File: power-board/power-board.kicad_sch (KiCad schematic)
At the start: 0 parts

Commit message: esp8266 module
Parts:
- added BT1: Battery_Cell, symbol Device:Battery_Cell
- added P1: USB_C_Plug_USB2.0, symbol Connector:USB_C_Plug_USB2.0
- added U1: AP9101CK6, Package_TO_SOT_SMD:SOT-23-6, symbol Battery_Management:AP9101CK6
- added U2: AP130-33Y, Package_TO_SOT_SMD:SOT-89-3, symbol Regulator_Linear:AP130-33Y
- added U3: MCP73831-3-OT, Package_TO_SOT_SMD:SOT-23-5, symbol Battery_Management:MCP73831-3-OT
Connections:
- new net: P1.A1 (GND), P1.A12 (GND), P1.B1 (GND), P1.B12 (GND)
- new net: P1.A4 (VBUS), P1.A9 (VBUS), P1.B4 (VBUS), P1.B9 (VBUS)

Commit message: initial diagram
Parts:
- added C1: 100n, symbol Device:C
- added C2: 1n, symbol Device:C
- added C3, C4: 4u7, symbol Device:C
- added C5: 1u, symbol Device:C
- added C6: 10u, symbol Device:C
- added C7, C8: 1000u, symbol Device:C_Polarized
- added F1: 2A slow, symbol Device:Fuse
- added J1: RGB matrix, symbol Connector_Generic:Conn_01x03
- added Q1, Q2: AOB2146L, Package_TO_SOT_SMD:TO-263-2, symbol Transistor_FET:IRFS4115
- added R1: 330, symbol Device:R
- added R10, R9: 5k1, symbol Device:R
- added R2: 2k7, symbol Device:R
- added R3: 1k, symbol Device:R
- added R4: 3k3, symbol Device:R
- added R5: 10k, symbol Device:R
- added R6: 100k, symbol Device:R
- added R7: LDR03, OptoDevice:R_LDR_10x8.5mm_P7.6mm_Vertical, symbol Sensor_Optical:LDR03
- added R8: 470, symbol Device:R
- added SW1: On, symbol Switch:SW_SPST
- added SW2: Mode, symbol Switch:SW_SPST
- added U4: ESP8266-NodeM, symbol rgb_matrix:ESP8266-NodeM
- BT1: value Battery_Cell -> 18650
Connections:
- net +3V3: now reaches U2.1 (VO)
- net +3V3: now also C6.1, C7.1, R5.1, R7.1, U4. (A0)
- net GND: now reaches U2.2 (GND)
- net GND: now also P1.A1 (GND), P1.A12 (GND), P1.B1 (GND), P1.B12 (GND), U3.2 (V_{SS}), C2.2, C3.2, C4.2, C5.2, C6.2, C7.2, C8.2, J1.1 (Pin_1), Q1.3 (S), R10.2, R2.2, R3.1, R4.2, R6.2, R9.2, SW2.1 (A), U4. (A0)
- net +VSW: now reaches U2.3 (VI)
- net +VSW: now also C5.1, C8.1, J1.3 (Pin_3), SW1.2 (B)
- net at BT1.1 (+): now also F1.2
- net BAT-: now reaches BT1.2 (-)
- net BAT-: now also U1.6 (VSS), C1.2, Q2.3 (S)
- net at P1.A4 (VBUS), P1.A9 (VBUS), P1.B4 (VBUS)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: now also U3.4 (V_{DD}), C3.1
- net at P1.A5 (CC): now also R10.1
- net at P1.B5 (VCONN): now also R9.1
- net at P1.SH (SHIELD): now also C2.1, R3.2
- net at U3.3 (V_{BAT}): now also C4.1, F1.1, R1.1, SW1.1 (A)
- net at U3.5 (PROG): now also R4.1
- net at U1.1 (DO): now also Q1.1 (G)
- net at U1.2 (VM): now also R2.1
- net at U1.3 (CO): now also Q2.1 (G)
- net at U1.5 (VDD): now also C1.1, R1.2
- new net: R6.1, R7.2, U4. (A0)
- new net: R5.2, SW2.2 (B), U4. (A0)
- new net: R8.2, U4. (A0)
- new net: Q1.2 (D), Q2.2 (D)
- new net: J1.2 (Pin_2), R8.1
- no-connect marks 0 -> 6
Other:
- note added: "Power must be directly connected to all four panels"
- note added: "Should mechanically block USB input when On"
- note added: "star ground"
- moved on the sheet: BT1, P1, U1, U2, U3

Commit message: esp legs
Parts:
- removed J1: RGB matrix, symbol Connector_Generic:Conn_01x03
- added J1: Conn_01x01, symbol Connector_Generic:Conn_01x01
- added J2, J3, J4, J5: Conn_01x02, symbol Connector_Generic:Conn_01x02
- C2: value 1n -> 1n/50V
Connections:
- net +3V3: now also U4.1 (3V3), U4.10 (3V3), U4.26 (3V3); no longer U4. (A0)
- net +VSW: now also J2.1 (Pin_1), J3.1 (Pin_1), J4.1 (Pin_1), J5.1 (Pin_1)
- net GND: now also U4.2 (GND), U4.25 (GND), U4.29 (GND), U4.9 (GND), J2.2 (Pin_2), J3.2 (Pin_2), J4.2 (Pin_2), J5.2 (Pin_2); no longer U4. (A0)
- net at R6.1, R7.2: now also U4.16 (A0); no longer U4. (A0)
- net at R5.2, SW2.2 (B): now also U4.14 (D1); no longer U4. (A0)
- net at R8.2: now also U4.13 (D2); no longer U4. (A0)
- net at R8.1: now also J1.1 (Pin_1)
- no-connect marks 6 -> 4
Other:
- moved on the sheet: C8

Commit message: usb
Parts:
- removed J1: Conn_01x01, symbol Connector_Generic:Conn_01x01
- removed J5: Conn_01x02, symbol Connector_Generic:Conn_01x02
- removed P1: USB_C_Plug_USB2.0, symbol Connector:USB_C_Plug_USB2.0
- added J1: USB_C, Connector_USB:USB_C_Receptacle_GCT_USB4125-xx-x-0190_6P_TopMnt_Horizontal, symbol Connector:USB_C_Receptacle_PowerOnly_6P
- added J6: Conn_01x03, TerminalBlock_Phoenix:TerminalBlock_Phoenix_PT-1,5-3-3.5-H_1x03_P3.50mm_Horizontal, symbol Connector_Generic:Conn_01x03
- BT1, J2, J3, J4: footprint (none) -> TerminalBlock_Phoenix:TerminalBlock_Phoenix_PT-1,5-2-5.0-H_1x02_P5.00mm_Horizontal
- C1, C2, C3, C4, C5, C6: footprint (none) -> Capacitor_SMD:C_0805_2012Metric_Pad1.18x1.45mm_HandSolder
- C7, C8: footprint (none) -> Capacitor_THT:CP_Radial_D12.5mm_P5.00mm
- F1: footprint (none) -> Fuse:Fuseholder_Cylinder-5x20mm_Schurter_0031_8201_Horizontal_Open
- R1, R10, R2, R3, R4, R5, R6, R8, R9: footprint (none) -> Resistor_SMD:R_0805_2012Metric_Pad1.20x1.40mm_HandSolder
- U4: footprint (none) -> RF_Module:ESP32-C3-DevKitM-1
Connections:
- net +VSW: now also J6.1 (Pin_1)
- net GND: now also J1.A12 (GND), J1.B12 (GND), J6.3 (Pin_3)
- net at R9.1: now also J1.B5 (CC2)
- net at R8.1: now also J6.2 (Pin_2)
- net at R10.1: now also J1.A5 (CC1)
- net at C2.1, R3.2: now also J1.SH (SHIELD)
- net at C3.1, U3.4 (V_{DD}): now also J1.A9 (VBUS), J1.B9 (VBUS)
- no-connect marks 4 -> 2
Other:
- moved on the sheet: C2, C7, R10, R3, R5, R6, R7, R8, R9, SW2, U4

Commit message: rough pcb layout
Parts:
- removed BT1: 18650, TerminalBlock_Phoenix:TerminalBlock_Phoenix_PT-1,5-2-5.0-H_1x02_P5.00mm_Horizontal, symbol Device:Battery_Cell
- removed SW2: Mode, symbol Switch:SW_SPST
- added C9: 100n, Capacitor_SMD:C_0805_2012Metric_Pad1.18x1.45mm_HandSolder, symbol Device:C
- added H1, H2: Bat, MountingHole:MountingHole_3.2mm_M3, symbol Mechanical:MountingHole
- added J5: Bat+, Connector_Pin:Pin_D1.3mm_L11.0mm, symbol Connector:Conn_01x01_Socket
- added J7: Bat-, Connector_Pin:Pin_D1.3mm_L11.0mm_LooseFit, symbol Connector:Conn_01x01_Socket
- added SW2: Mode, Button_Switch_THT:SW_Push_2P1T_Toggle_CK_PVA1xxH1xxxxxxV2, symbol Switch:SW_MEC_5E
- added TP1: BAT+, TestPoint:TestPoint_Pad_2.0x2.0mm, symbol Connector:TestPoint
- added TP3: 3V3, TestPoint:TestPoint_Pad_2.0x2.0mm, symbol Connector:TestPoint
- added TP4: BAT-, TestPoint:TestPoint_Pad_2.0x2.0mm, symbol Connector:TestPoint
- added TP5: Gnd, TestPoint:TestPoint_Pad_2.0x2.0mm, symbol Connector:TestPoint
- C7, C8: footprint Capacitor_THT:CP_Radial_D12.5mm_P5.00mm -> Capacitor_THT:CP_Radial_D10.0mm_P5.00mm
- J2, J3, J4: footprint TerminalBlock_Phoenix:TerminalBlock_Phoenix_PT-1,5-2-5.0-H_1x02_P5.00mm_Horizontal -> Connector_PinHeader_2.54mm:PinHeader_2x01_P2.54mm_Vertical
- J6: footprint TerminalBlock_Phoenix:TerminalBlock_Phoenix_PT-1,5-3-3.5-H_1x03_P3.50mm_Horizontal -> Connector_PinHeader_2.54mm:PinHeader_1x03_P2.54mm_Vertical
- SW1: footprint (none) -> Connector_PinHeader_2.54mm:PinHeader_2x01_P2.54mm_Vertical
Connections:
- net +3V3: now also TP3.1
- net +VSW: now also J2.2 (Pin_2), J3.2 (Pin_2), J4.2 (Pin_2), J6.3 (Pin_3), TP1.1; no longer J2.1 (Pin_1), J3.1 (Pin_1), J4.1 (Pin_1), J6.1 (Pin_1)
- net BAT-: now also J7.1 (Pin_1), TP4.1
- net GND: now also J2.1 (Pin_1), J3.1 (Pin_1), J4.1 (Pin_1), J6.1 (Pin_1), C9.1, SW2.1, TP5.1; no longer J2.2 (Pin_2), J3.2 (Pin_2), J4.2 (Pin_2), J6.3 (Pin_3)
- net at F1.2: now also J5.1 (Pin_1)
- net at R5.2, U4.14 (D1): now also C9.2, SW2.4 (A)
- no-connect marks 2 -> 4
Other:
- note added: "18650 Cell"
- moved on the sheet: J2, J3, J4, J6, R5

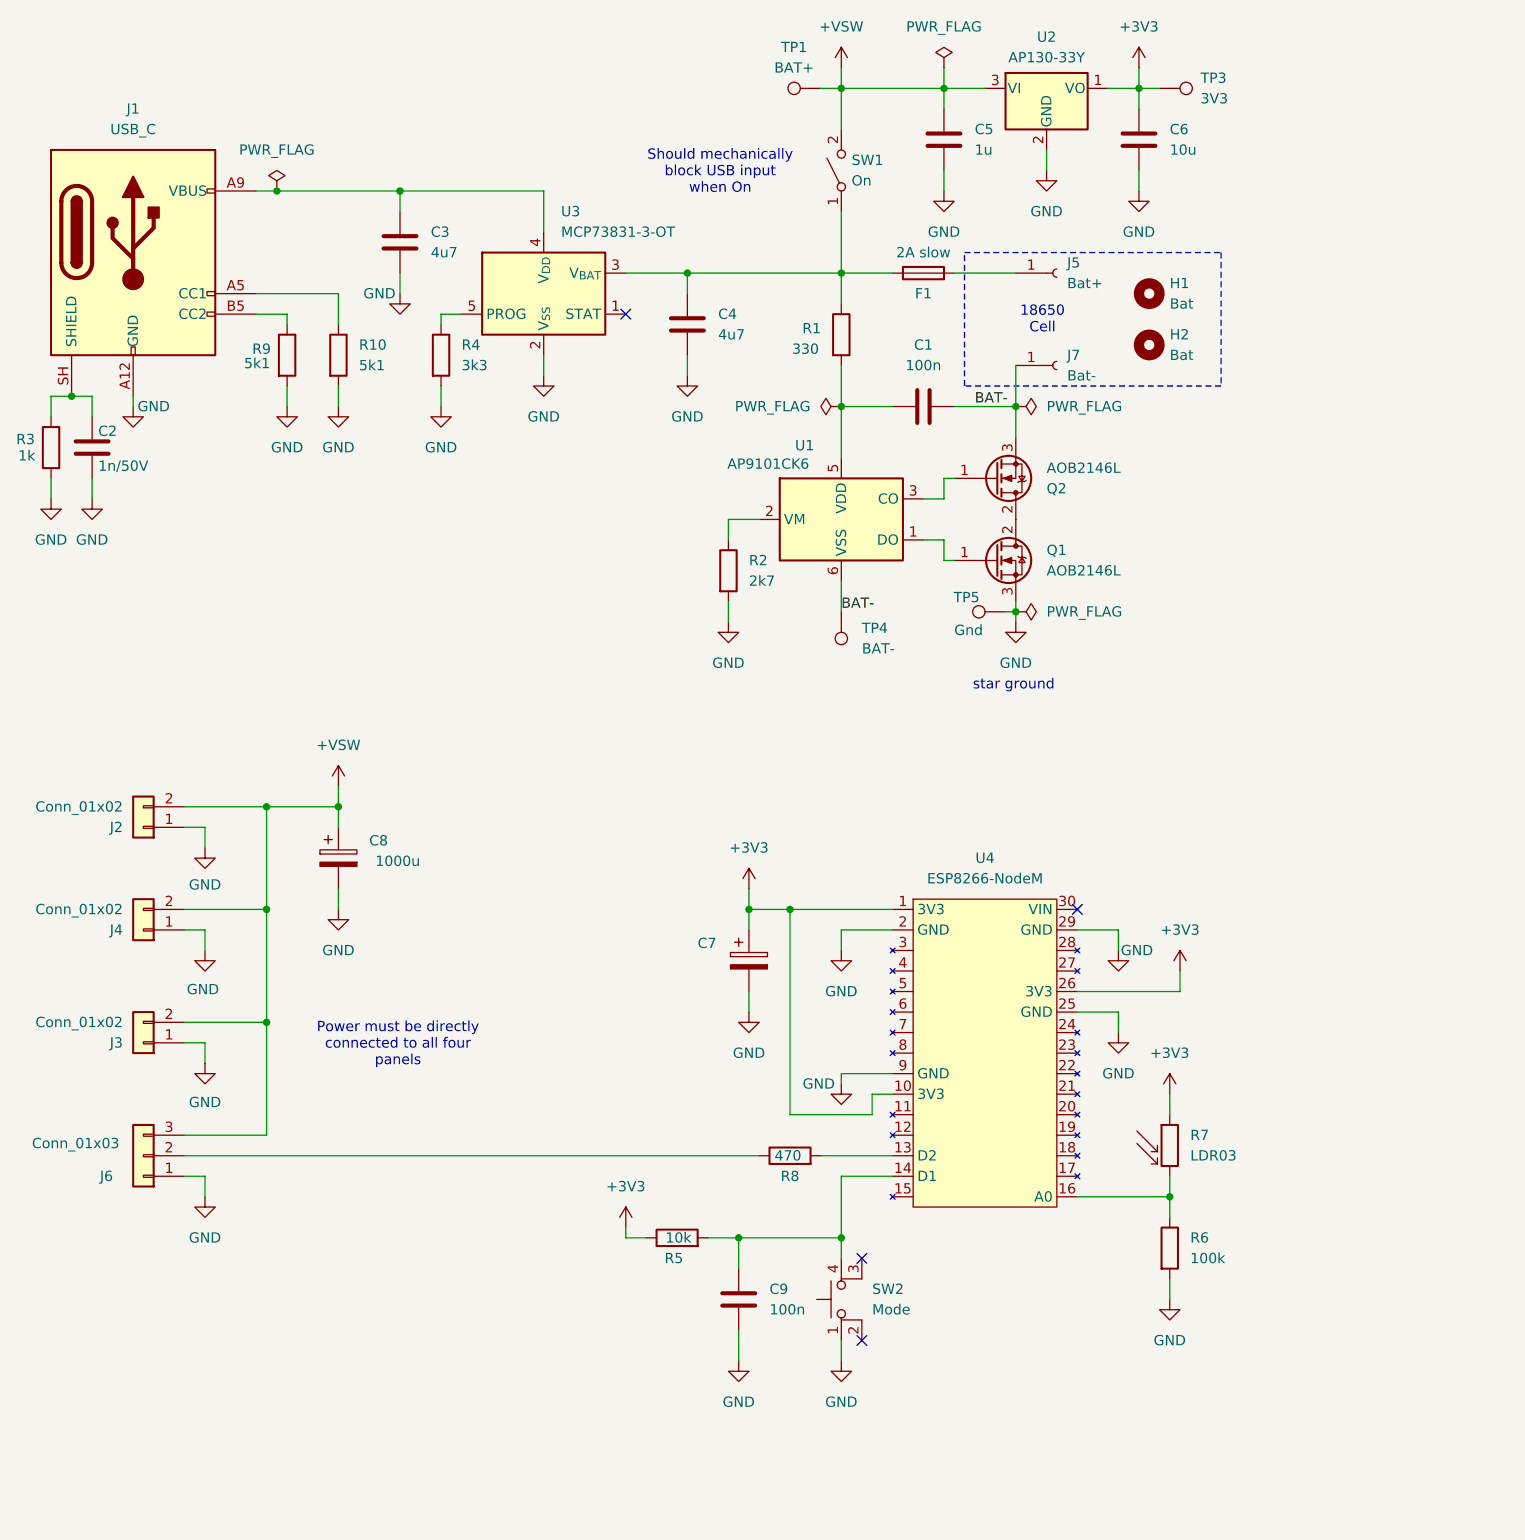
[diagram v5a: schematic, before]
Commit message: inrush limiting / soft start & orientation of dev board
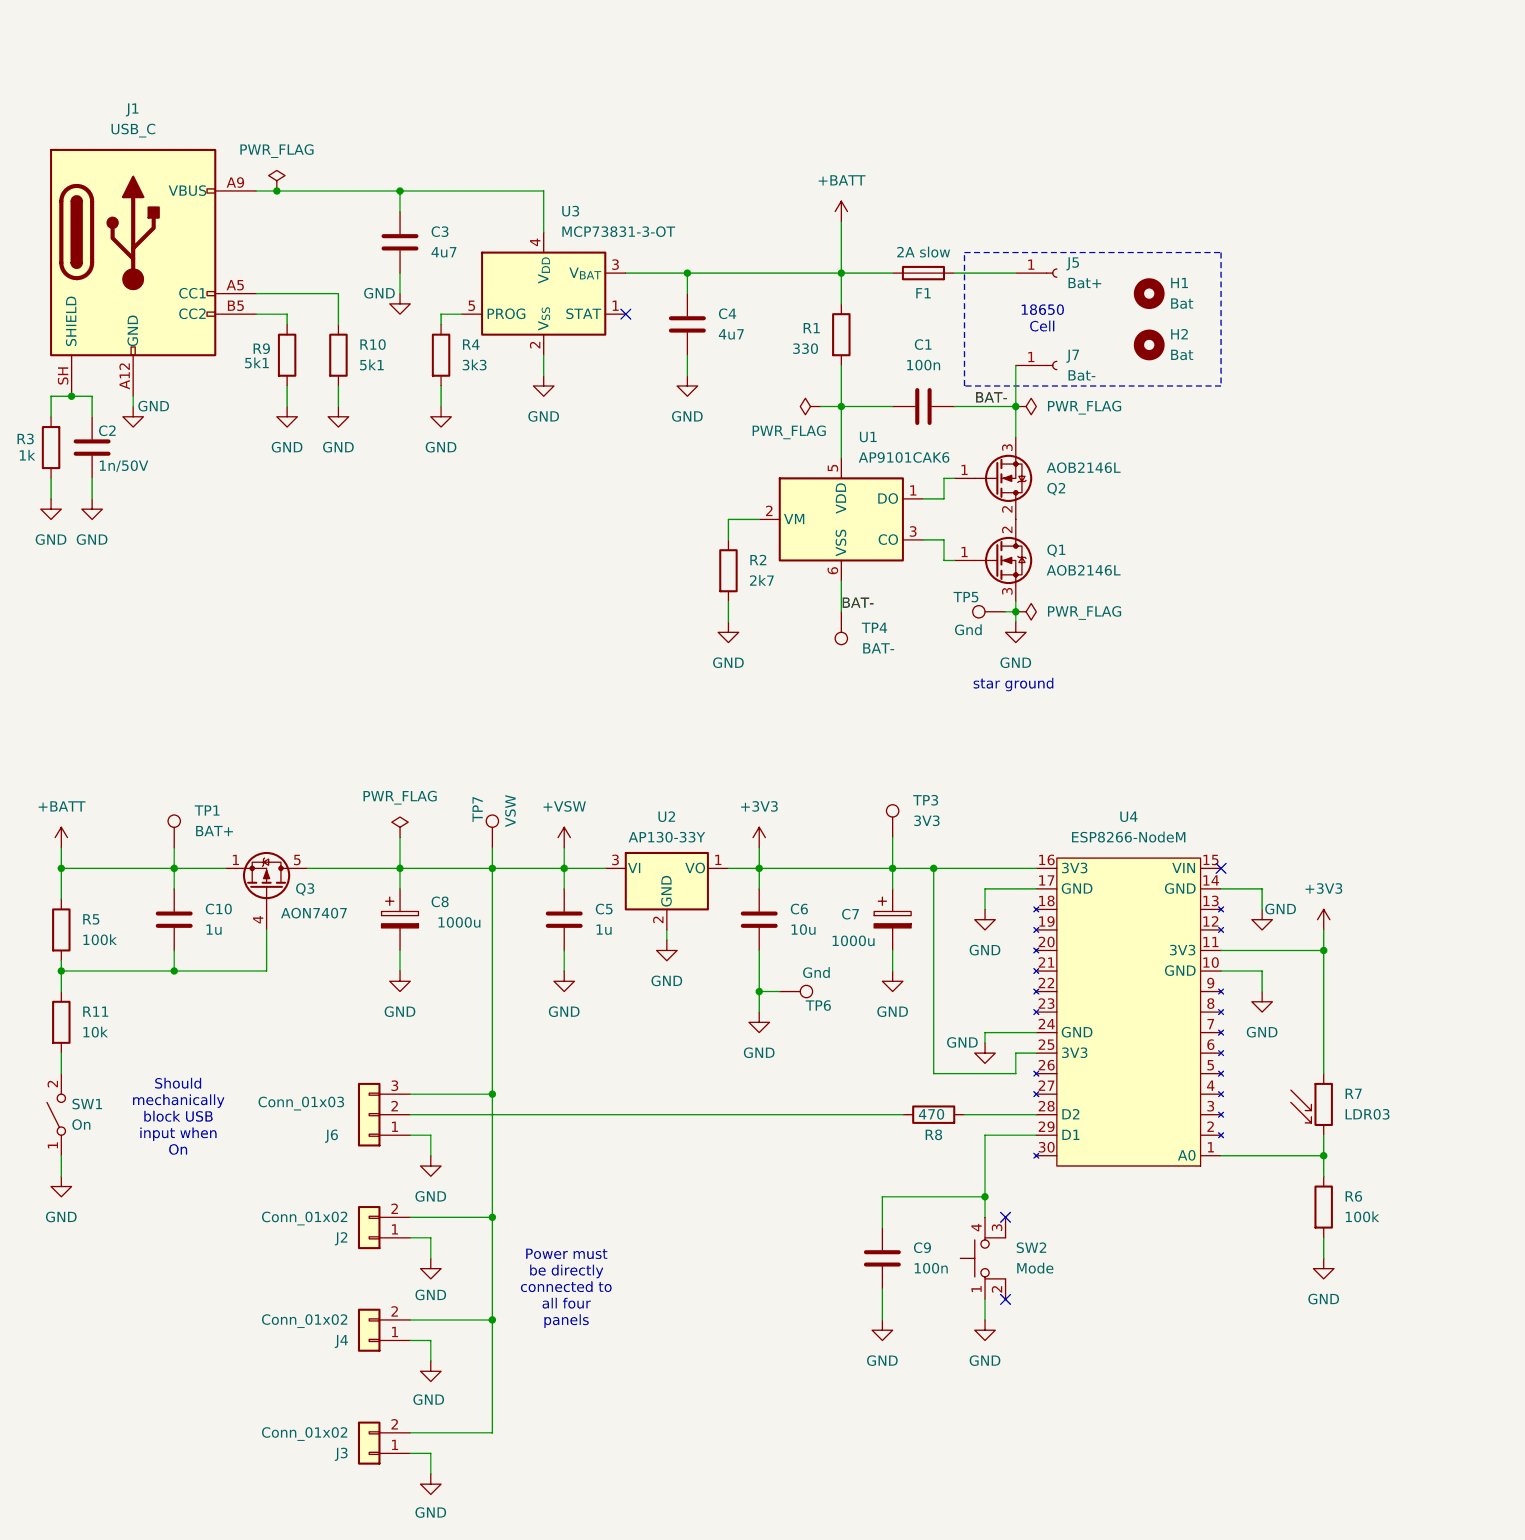
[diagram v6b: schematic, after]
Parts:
- removed U1: AP9101CK6, Package_TO_SOT_SMD:SOT-23-6, symbol Battery_Management:AP9101CK6
- added C10: 1u, Capacitor_SMD:C_0805_2012Metric_Pad1.18x1.45mm_HandSolder, symbol Device:C
- added Q3: AON7407, Package_DFN_QFN:AO_DFN-8-1EP_5.55x5.2mm_P1.27mm_EP4.12x4.6mm, symbol Transistor_FET:AON6411
- added R11: 10k, Resistor_SMD:R_0805_2012Metric_Pad1.20x1.40mm_HandSolder, symbol Device:R
- added TP6: Gnd, TestPoint:TestPoint_Pad_2.0x2.0mm, symbol Connector:TestPoint
- added TP7: VSW, TestPoint:TestPoint_Pad_2.0x2.0mm, symbol Connector:TestPoint
- added U1: AP9101CAK6, Package_TO_SOT_SMD:SOT-23-6, symbol rgb_matrix:AP9101CAK6
- J5: footprint Connector_Pin:Pin_D1.3mm_L11.0mm -> Connector_Pin:Pin_D1.3mm_L11.0mm_LooseFit
- R5: value 10k -> 100k
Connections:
- net +3V3: now also U4.11 (3V3), U4.16 (3V3), U4.25 (3V3); no longer R5.1, U4.1 (3V3), U4.10 (3V3), U4.26 (3V3)
- net +VSW: now also Q3.5 (D), TP7.1; no longer SW1.2 (B), TP1.1
- net BAT-: now also U1.6 (VSS)
- net GND: now also SW1.1 (A), U4.10 (GND), U4.14 (GND), U4.17 (GND), U4.24 (GND), TP6.1; no longer U4.2 (GND), U4.25 (GND), U4.29 (GND), U4.9 (GND)
- net +BATT: now reaches C4.1, F1.1, R1.1, U3.3 (V_{BAT})
- net +BATT: now also R5.1, TP1.1, C10.1, Q3.1 (S), Q3.2 (S), Q3.3 (S); no longer SW1.1 (A)
- net at C9.2, SW2.4 (A): now also U4.29 (D1); no longer R5.2, U4.14 (D1)
- net at Q2.1 (G): now also U1.1 (DO)
- net at Q1.1 (G): now also U1.3 (CO)
- net at R6.1, R7.2: now also U4.1 (A0); no longer U4.16 (A0)
- net at C1.1, R1.2: now also U1.5 (VDD)
- net at R2.1: now also U1.2 (VM)
- net at U4.13: no longer R8.2
- net at U4.28 (D2): now also R8.2
- new net: C10.2, Q3.4 (G), R11.1, R5.2
- new net: R11.2, SW1.2 (B)
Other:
- moved on the sheet: C5, C6, C8, C9, J2, J3, J4, J6, R6, R7, R8, SW1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

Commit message: v1
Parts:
- J2: value Conn_01x02 -> - +
- J3, J4: value Conn_01x02 -> + -
- J6: value Conn_01x03 -> - In +
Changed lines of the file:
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@@
 			)
 		)
-		(property "Value" "Conn_01x02"
+		(property "Value" "+ -"
 			(at 58.42 208.2801 0)
 			(show_name no)
@@
 			)
 		)
-		(property "Value" "Conn_01x02"
+		(property "Value" "+ -"
 			(at 58.42 222.2501 0)
 			(show_name no)
@@
 			)
 		)
-		(property "Value" "Conn_01x02"
+		(property "Value" "- +"
 			(at 58.42 195.5801 0)
 			(show_name no)
@@
 			)
 		)
-		(property "Value" "Conn_01x03"
-			(at 52.578 181.356 0)
+		(property "Value" "- In +"
+			(at 56.134 180.848 0)
 			(show_name no)
 			(do_not_autoplace no)
